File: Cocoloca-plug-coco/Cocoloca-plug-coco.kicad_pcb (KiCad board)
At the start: 2 copper layers, 1 part

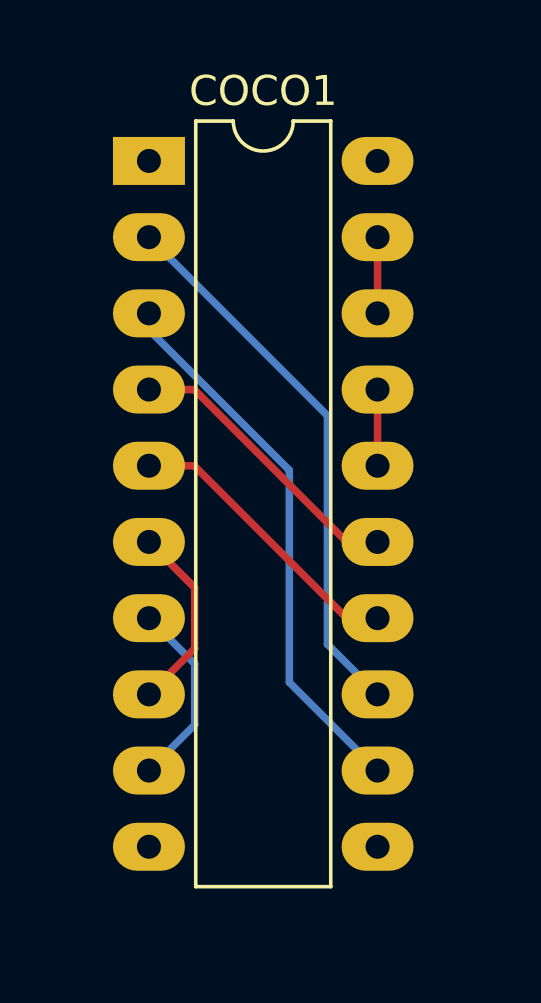
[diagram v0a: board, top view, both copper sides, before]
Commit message: Gerbers cleaned up
Added missing edge cuts for Coco1 plug. Added dxf graphic files and cleaned up gerber plots as per board house production specs.
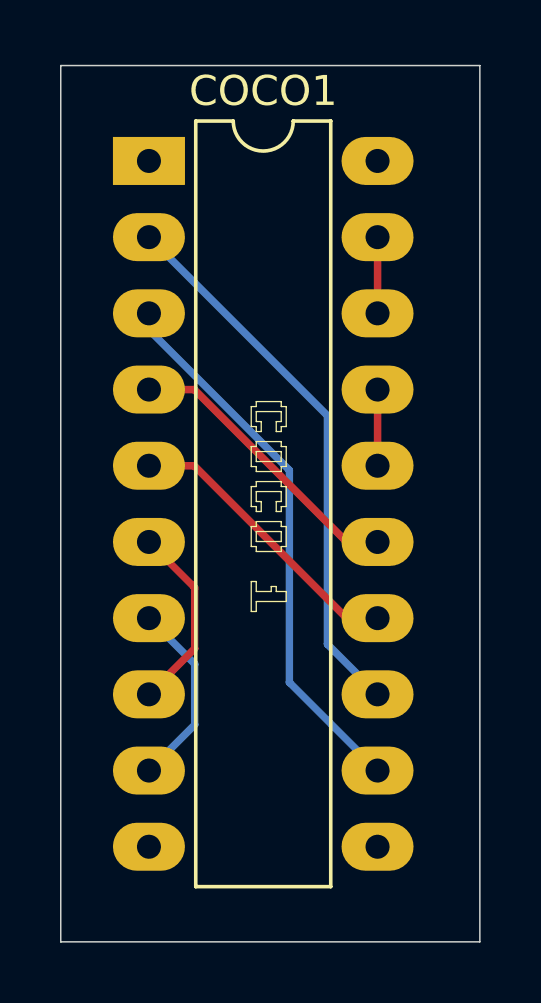
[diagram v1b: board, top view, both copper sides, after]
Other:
- board outline added: 14 x 29.2 mm
